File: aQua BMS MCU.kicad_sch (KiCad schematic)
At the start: 29 parts, among them SW1 SW_Push, U2 STM32F205RETx

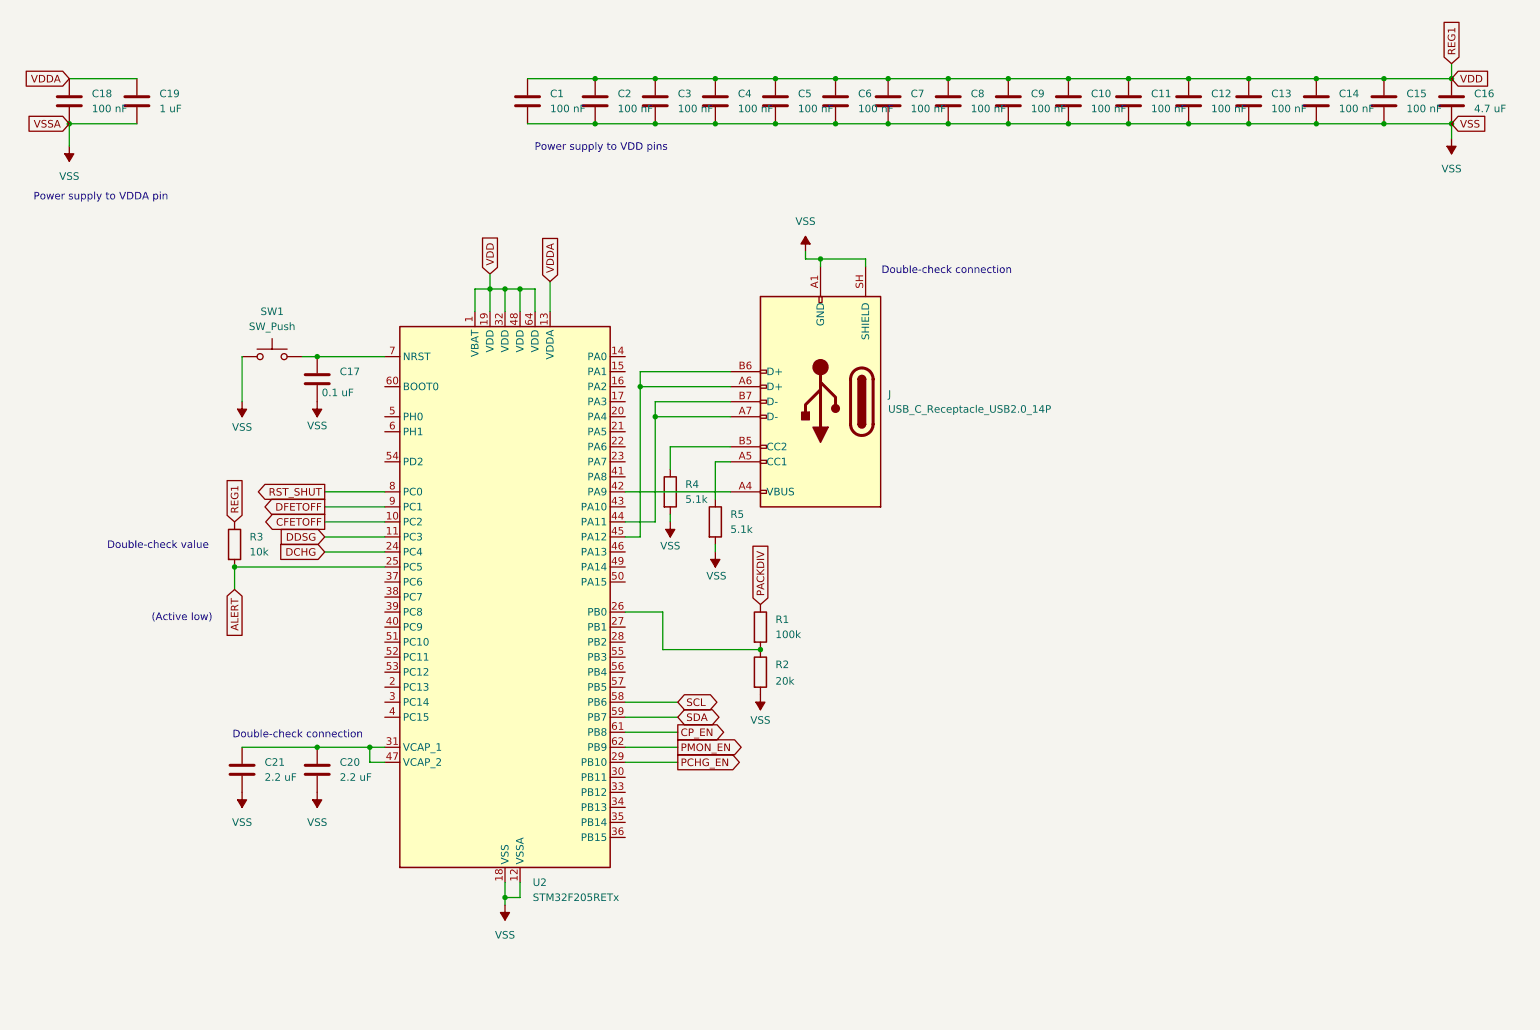
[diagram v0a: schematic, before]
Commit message: aQua BMS MCU Updated June 4
Fixed? VCAP1 and VCAP2 connections, added BOOT0 pin connection
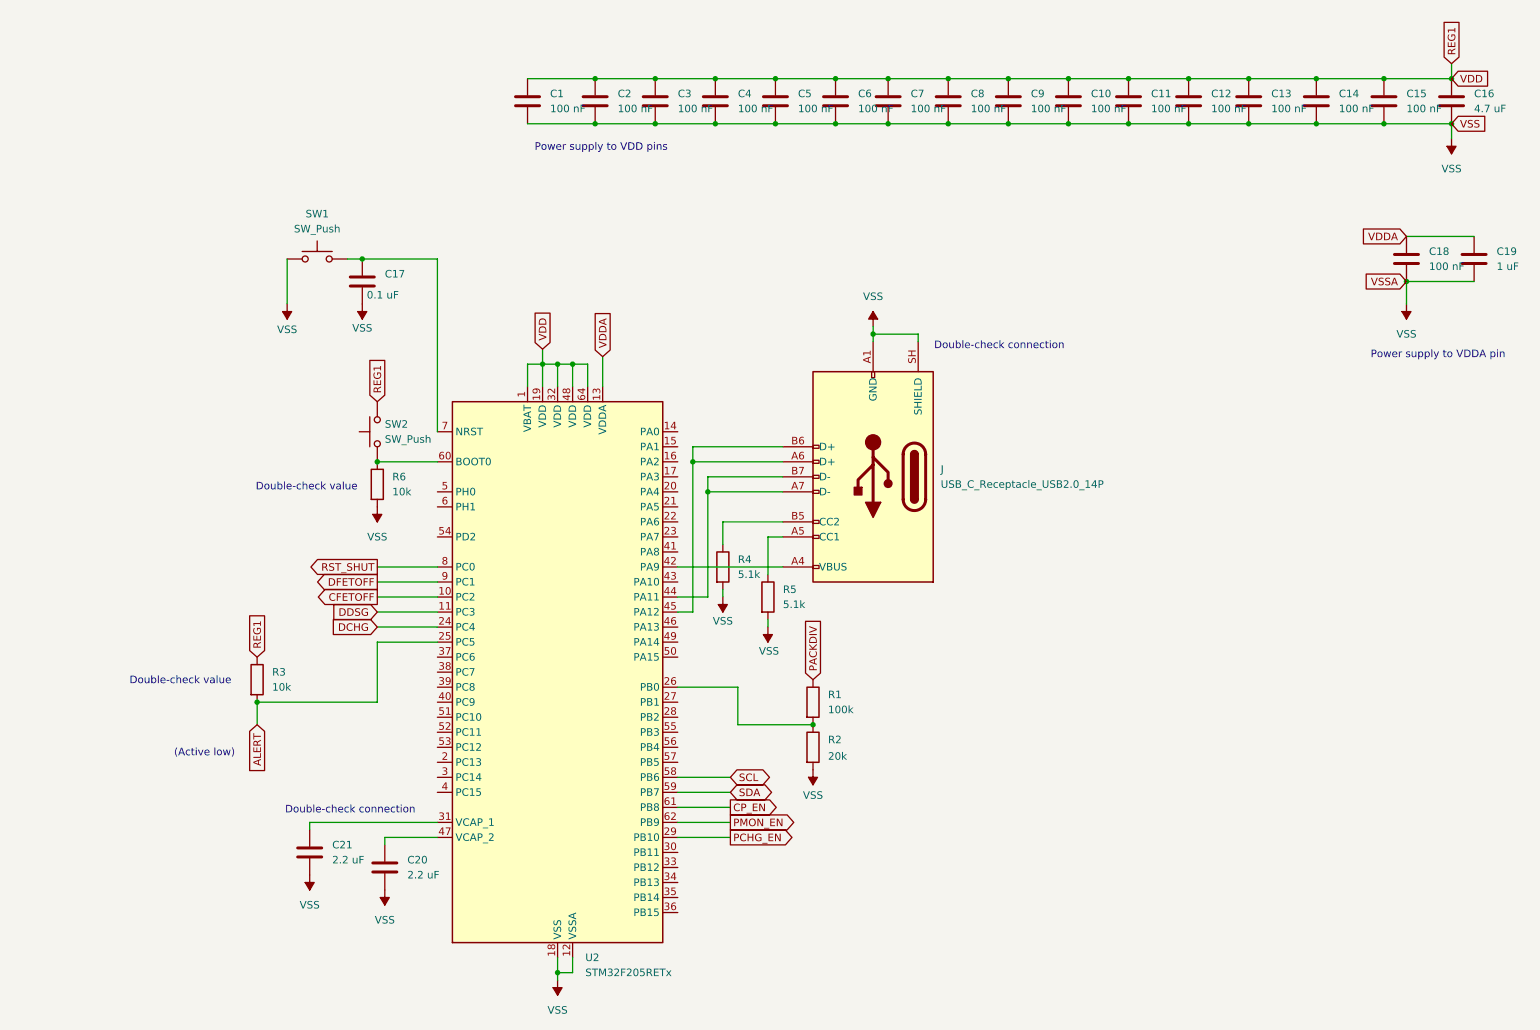
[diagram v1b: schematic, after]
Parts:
- added R6: 10k, symbol Device:R
- added SW2: SW_Push, symbol Switch:SW_Push
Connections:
- net REG1: now also SW2.2
- net VSS: now also R6.2
- net at C20.1, U2.47 (VCAP_2): no longer C21.1, U2.31 (VCAP_1)
- net at U2.60 (BOOT0): now also R6.1, SW2.1
- new net: C21.1, U2.31 (VCAP_1)
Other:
- moved on the sheet: C17, C18, C19, C20, C21, J, R1, R2, R3, R4, R5, SW1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
